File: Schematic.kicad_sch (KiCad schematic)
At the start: 37 parts, among them J1 Screw_Terminal_01x04, Q1 HY1707, Q2 HY1707, Q3 S8050, U1 UC2843A

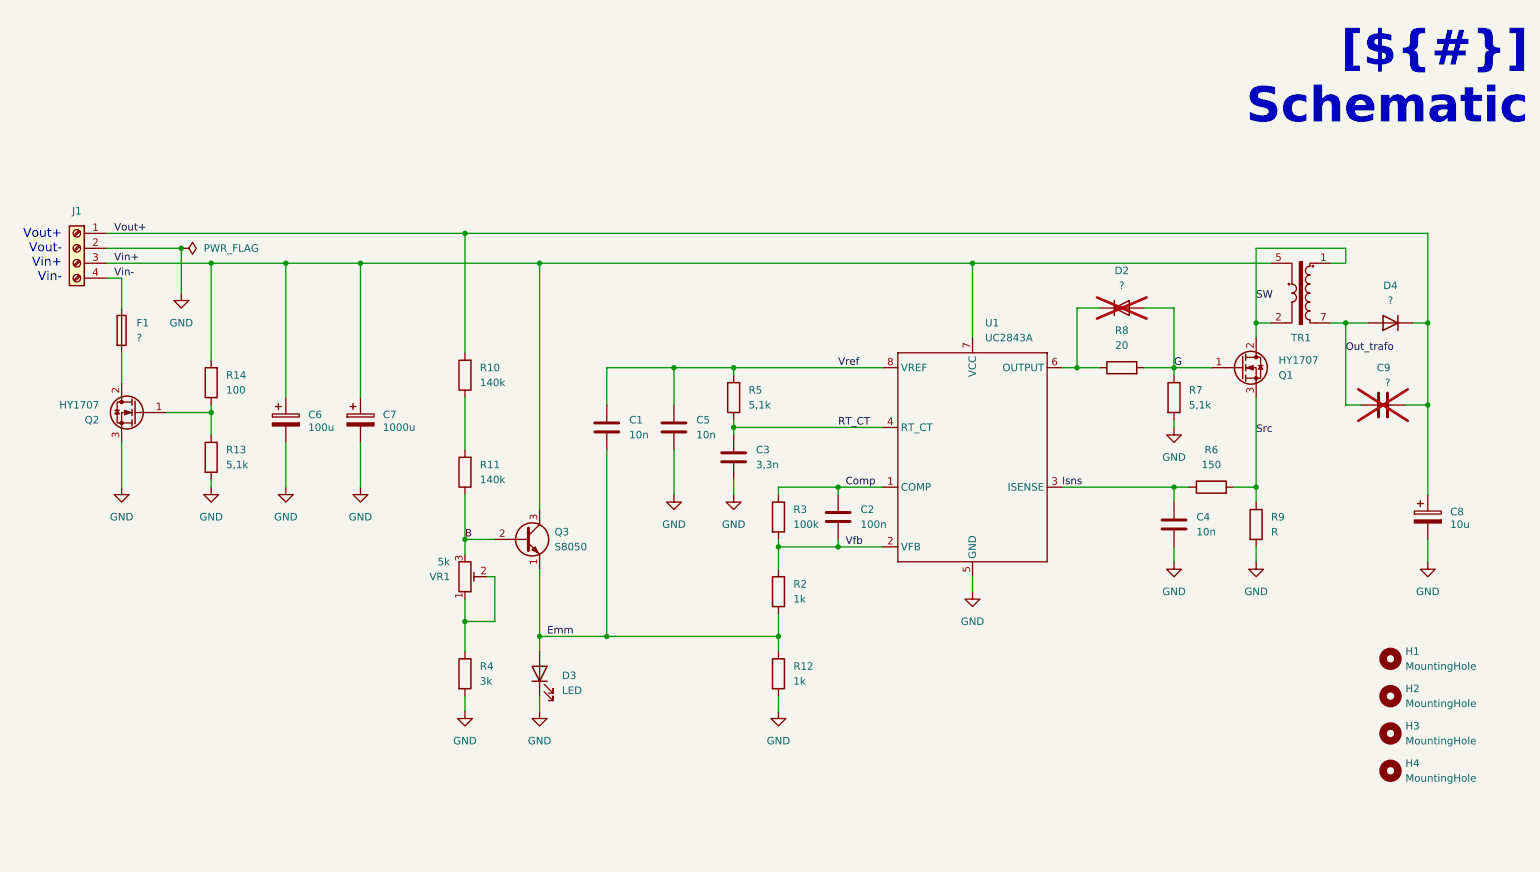
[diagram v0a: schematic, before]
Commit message: Added notes for unidentified parts
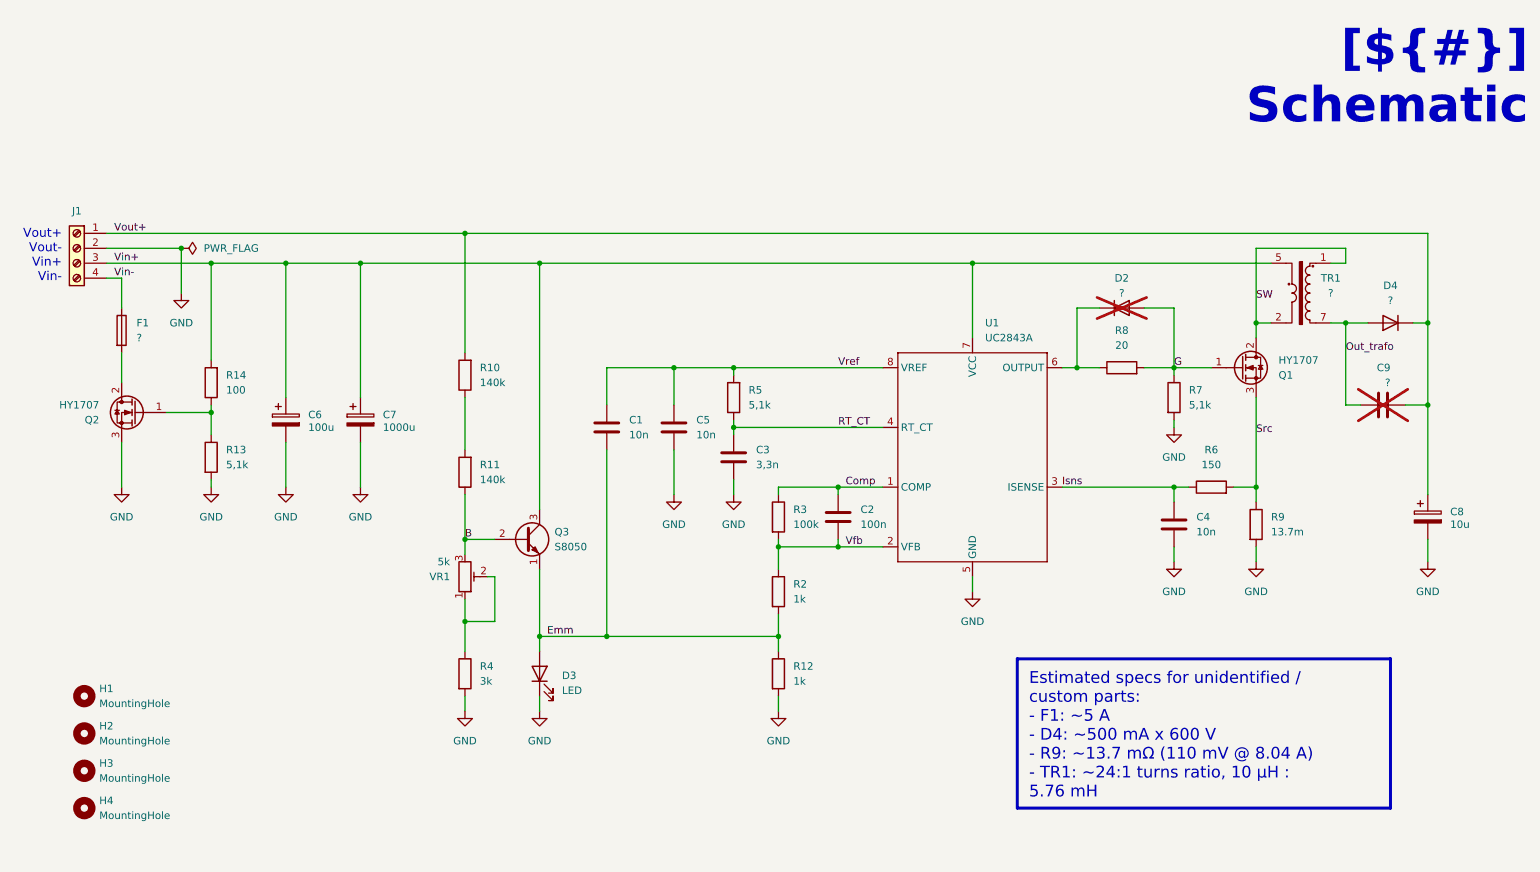
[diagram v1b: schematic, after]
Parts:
- R9: value R -> 13.7m
- TR1: value ~ -> ?
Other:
- moved on the sheet: H1, H2, H3, H4
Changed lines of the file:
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@@
 		)
 	)
+	(text_box "Estimated specs for unidentified / custom parts:\n- F1: ~5 A\n- D4: ~500 mA x 600 V\n- R9: ~13.7 mΩ (110 mV @ 8.04 A)\n- TR1: ~24:1 turns ratio, 10 μH : 5.76 mH"
+		(exclude_from_sim no)
+		(at 190.5 120.65 0)
+		(size 63.5 25.4)
+		(margins 2 2 2 2)
+		(stroke
+			(width 0.508)
+			(type solid)
+			(color 132 132 132 1)
+		)
+		(fill
+			(type color)
+			(color 200 200 200 1)
+		)
+		(effects
+			(font
+				(face "Arial")
+				(size 2 2)
+				(color 0 0 0 1)
+			)
+			(justify left top)
+		)
+	)
 	(junction
 		(at 53.34 53.34)
@@
 		(dnp no)
 		(property "Reference" "TR1"
-			(at 238.76 66.04 0)
+			(at 243.84 55.88 0)
 			(effects
 				(font
@@
 			)
 		)
-		(property "Value" "~"
-			(at 238.7219 50.8 0)
+		(property "Value" "?"
+			(at 243.84 58.42 0)
 			(effects
 				(font
 					(size 1.27 1.27)
 				)
-				(hide yes)
 			)
 		)
@@
 	(symbol
 		(lib_id "Mechanical:MountingHole")
-		(at 254 120.65 0)
+		(at 31.75 127 0)
 		(unit 1)
 		(exclude_from_sim no)
@@
 		(fields_autoplaced yes)
 		(property "Reference" "H1"
-			(at 256.54 119.3799 0)
+			(at 34.29 125.7299 0)
 			(effects
 				(font
@@
 		)
 		(property "Value" "MountingHole"
-			(at 256.54 121.9199 0)
+			(at 34.29 128.2699 0)
 			(effects
 				(font
@@
 		)
 		(property "Footprint" "MountingHole:MountingHole_2.1mm"
-			(at 254 120.65 0)
+			(at 31.75 127 0)
 			(effects
 				(font
@@
 		)
 		(property "Datasheet" "~"
-			(at 254 120.65 0)
+			(at 31.75 127 0)
 			(effects
 				(font
@@
 		)
 		(property "Description" "Mounting Hole without connection"
-			(at 254 120.65 0)
+			(at 31.75 127 0)
 			(effects
 				(font
@@
 	(symbol
 		(lib_id "Mechanical:MountingHole")
-		(at 254 139.7 0)
+		(at 31.75 146.05 0)
 		(unit 1)
 		(exclude_from_sim no)
@@
 		(fields_autoplaced yes)
 		(property "Reference" "H4"
-			(at 256.54 138.4299 0)
+			(at 34.29 144.7799 0)
 			(effects
 				(font
@@
 		)
 		(property "Value" "MountingHole"
-			(at 256.54 140.9699 0)
+			(at 34.29 147.3199 0)
 			(effects
 				(font
@@
 		)
 		(property "Footprint" "MountingHole:MountingHole_2.1mm"
-			(at 254 139.7 0)
+			(at 31.75 146.05 0)
 			(effects
 				(font
@@
 		)
 		(property "Datasheet" "~"
-			(at 254 139.7 0)
+			(at 31.75 146.05 0)
 			(effects
 				(font
@@
 		)
 		(property "Description" "Mounting Hole without connection"
-			(at 254 139.7 0)
+			(at 31.75 146.05 0)
 			(effects
 				(font
@@
 	(symbol
 		(lib_id "Mechanical:MountingHole")
-		(at 254 127 0)
+		(at 31.75 133.35 0)
 		(unit 1)
 		(exclude_from_sim no)
@@
 		(fields_autoplaced yes)
 		(property "Reference" "H2"
-			(at 256.54 125.7299 0)
+			(at 34.29 132.0799 0)
 			(effects
 				(font
@@
 		)
 		(property "Value" "MountingHole"
-			(at 256.54 128.2699 0)
+			(at 34.29 134.6199 0)
 			(effects
 				(font
@@
 		)
 		(property "Footprint" "MountingHole:MountingHole_2.1mm"
-			(at 254 127 0)
+			(at 31.75 133.35 0)
 			(effects
 				(font
@@
 		)
 		(property "Datasheet" "~"
-			(at 254 127 0)
+			(at 31.75 133.35 0)
 			(effects
 				(font
@@
 		)
 		(property "Description" "Mounting Hole without connection"
-			(at 254 127 0)
+			(at 31.75 133.35 0)
 			(effects
 				(font
@@
 		(on_board yes)
 		(dnp yes)
-		(fields_autoplaced yes)
 		(property "Reference" "D2"
-			(at 208.28 54.61 0)
+			(at 208.28 55.88 0)
 			(effects
 				(font
@@
 		)
 		(property "Value" "?"
-			(at 208.28 57.15 0)
+			(at 208.28 58.42 0)
 			(effects
 				(font
@@
 			)
 		)
-		(property "Value" "R"
+		(property "Value" "13.7m"
 			(at 233.68 99.0599 0)
 			(effects
@@
 	(symbol
 		(lib_id "Mechanical:MountingHole")
-		(at 254 133.35 0)
+		(at 31.75 139.7 0)
 		(unit 1)
 		(exclude_from_sim no)
@@
 		(fields_autoplaced yes)
 		(property "Reference" "H3"
-			(at 256.54 132.0799 0)
+			(at 34.29 138.4299 0)
 			(effects
 				(font
@@
 		)
 		(property "Value" "MountingHole"
-			(at 256.54 134.6199 0)
+			(at 34.29 140.9699 0)
 			(effects
 				(font
@@
 		)
 		(property "Footprint" "MountingHole:MountingHole_2.1mm"
-			(at 254 133.35 0)
+			(at 31.75 139.7 0)
 			(effects
 				(font
@@
 		)
 		(property "Datasheet" "~"
-			(at 254 133.35 0)
+			(at 31.75 139.7 0)
 			(effects
 				(font
@@
 		)
 		(property "Description" "Mounting Hole without connection"
-			(at 254 133.35 0)
+			(at 31.75 139.7 0)
 			(effects
 				(font

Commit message: Updated switcher IC
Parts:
- removed U1: UC2843A, Package_DIP:DIP-8_W7.62mm, symbol personal:UC2843AQD8R
- added U1: UC3845, Package_DIP:DIP-8_W7.62mm, symbol personal:UC3845
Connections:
- net Comp: now also U1.1 (COMP)
- net GND: now also U1.5 (GND)
- net Isns: now also U1.3 (ISENSE)
- net RT_CT: now also U1.4 (RT_CT)
- net Vfb: now also U1.2 (VFB)
- net Vin+: now also U1.7 (VCC)
- net Vref: now also U1.8 (VREF)
- net at D2.1 (K), R8.1: now also U1.6 (OUTPUT)
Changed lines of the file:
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@@
 		)
 	)
-	(text_box "Estimated specs for unidentified / custom parts:\n- F1: ~5 A\n- D4: ~500 mA x 600 V\n- R9: ~13.7 mΩ (110 mV @ 8.04 A)\n- TR1: ~24:1 turns ratio, 10 μH : 5.76 mH"
+	(text_box "Estimated specs for unidentified / custom parts:\n- F1: ~5 A\n- D4: ~500 mA x 600 V\n- R9: ~13.7 mΩ (110 mV @ 8.04 A)\n- TR1: ~1 : 19 turns ratio, 3.54 μH : 1.45 mH\n\nSee \"Supporting Docs\\Measurements.xlsx\" for details"
 		(exclude_from_sim no)
 		(at 190.5 120.65 0)
-		(size 63.5 25.4)
+		(size 63.5 31.115)
 		(margins 2 2 2 2)
 		(stroke
@@
 	)
 	(symbol
-		(lib_id "personal:UC2843AQD8R")
-		(at 182.88 86.36 0)
-		(unit 1)
-		(exclude_from_sim no)
-		(in_bom yes)
-		(on_board yes)
-		(dnp no)
-		(fields_autoplaced yes)
-		(property "Reference" "U1"
-			(at 185.0233 63.5 0)
-			(effects
-				(font
-					(size 1.27 1.27)
-				)
-				(justify left)
-			)
-		)
-		(property "Value" "UC2843A"
-			(at 185.0233 66.04 0)
-			(effects
-				(font
-					(size 1.27 1.27)
-				)
-				(justify left)
-			)
-		)
-		(property "Footprint" "Package_DIP:DIP-8_W7.62mm"
-			(at 198.12 105.41 0)
-			(effects
-				(font
-					(size 1.27 1.27)
-				)
-				(hide yes)
-			)
-		)
-		(property "Datasheet" ""
-			(at 182.88 86.36 0)
-			(effects
-				(font
-					(size 1.27 1.27)
-				)
-				(hide yes)
-			)
-		)
-		(property "Description" ""
-			(at 182.88 86.36 0)
-			(effects
-				(font
-					(size 1.27 1.27)
-				)
-				(hide yes)
-			)
-		)
-		(pin "5"
-		)
-		(pin "8"
-		)
-		(pin "1"
-		)
-		(pin "2"
-		)
-		(pin "4"
-		)
-		(pin "7"
-		)
-		(pin "3"
-		)
-		(pin "6"
-		)
-		(instances
-			(project ""
-				(path "/f9e05184-c88b-4a88-ae9c-ab2bdb32be7c/82da9dbf-ba38-4d08-ba35-a220fa2963b1/b0fdce11-0fa7-4399-9147-4b60eb490e1b"
-					(reference "U1")
-					(unit 1)
-				)
-			)
-		)
-	)
-	(symbol
 		(lib_id "Mechanical:MountingHole")
 		(at 31.75 146.05 0)
@@
 					(unit 1)
 				)
+			)
+		)
+	)
+	(symbol
+		(lib_id "personal:UC3845")
+		(at 182.88 86.36 0)
+		(unit 1)
+		(exclude_from_sim no)
+		(in_bom yes)
+		(on_board yes)
+		(dnp no)
+		(fields_autoplaced yes)
+		(property "Reference" "U1"
+			(at 185.0233 63.5 0)
+			(effects
+				(font
+					(size 1.27 1.27)
+				)
+				(justify left)
+			)
+		)
+		(property "Value" "UC3845"
+			(at 185.0233 66.04 0)
+			(effects
+				(font
+					(size 1.27 1.27)
+				)
+				(justify left)
+			)
+		)
+		(property "Footprint" "Package_DIP:DIP-8_W7.62mm"
+			(at 198.12 105.41 0)
+			(effects
+				(font
+					(size 1.27 1.27)
+				)
+				(hide yes)
+			)
+		)
+		(property "Datasheet" ""
+			(at 182.88 86.36 0)
+			(effects
+				(font
+					(size 1.27 1.27)
+				)
+				(hide yes)
+			)
+		)
+		(property "Description" ""
+			(at 182.88 86.36 0)
+			(effects
+				(font
+					(size 1.27 1.27)
+				)
+				(hide yes)
+			)
+		)
+		(pin "4"
+		)
+		(pin "8"
+		)
+		(pin "7"
+		)
+		(pin "6"
+		)
+		(pin "2"
+		)
+		(pin "5"
+		)
+		(pin "3"
+		)
+		(pin "1"
+		)
+		(instances
+			(project ""
+				(path "/f9e05184-c88b-4a88-ae9c-ab2bdb32be7c/82da9dbf-ba38-4d08-ba35-a220fa2963b1/b0fdce11-0fa7-4399-9147-4b60eb490e1b"
+					(reference "U1")
+					(unit 1)
+				)
